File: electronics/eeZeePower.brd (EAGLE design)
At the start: 25.9 x 12.7 mm, 12 parts

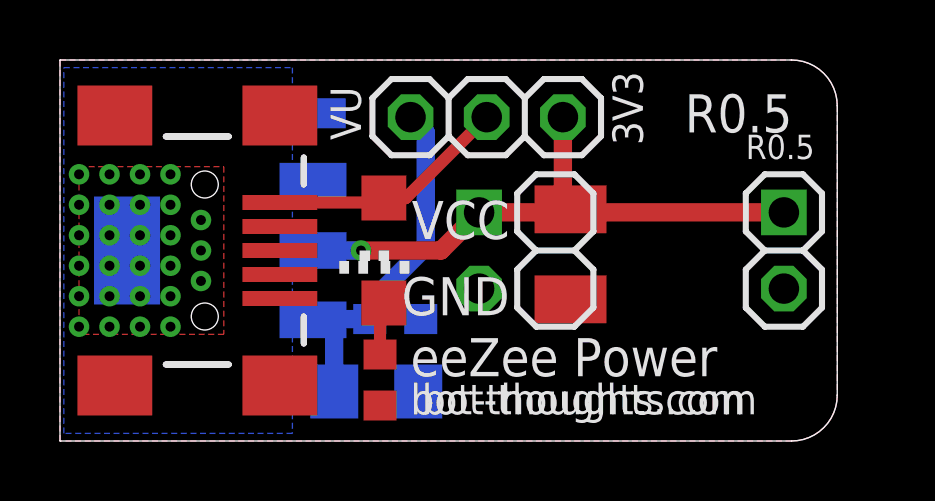
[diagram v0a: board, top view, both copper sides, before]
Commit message: modified logo to polygons, arcs; minor tweaks, moved url
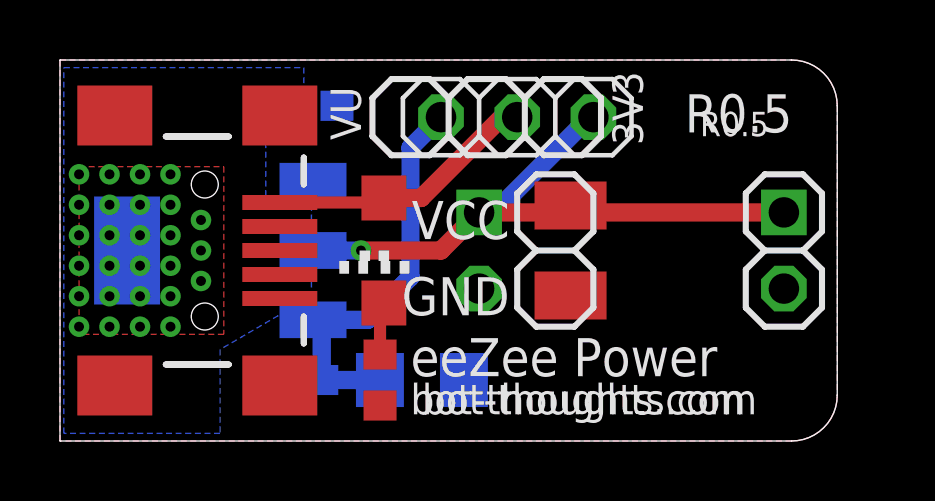
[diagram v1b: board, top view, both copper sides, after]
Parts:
- removed U$3: BOT-THOUGHTS-LOGO-MD, bt:BTLOGOM
- added U$2: BTLOGO-LOGO-MD, bt:BTLOGOM
- moved C2 3.88 mm to (7.87, 2.03), turned to 0 degrees
- moved C1 1.57 mm to (12.1, 2.03)
- moved JP10 1.02 mm to (15.2, 10.8)
- moved C3 0.36 mm to (8.38, 11.2)
- moved C4 0.13 mm to (17.0, 6.35)
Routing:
- net VOUT: track 20.4 -> 22.4 mm
- net VIN: track 12.6 -> 13.7 mm
- net VBUS: track 8.08 -> 9.09 mm
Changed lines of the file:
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@@
 <setting verticaltext="up"/>
 </settings>
-<grid distance="0.8" unitdist="mil" unit="mil" style="lines" multiple="1" display="yes" altdistance="0.01" altunitdist="inch" altunit="inch"/>
+<grid distance="0.005" unitdist="inch" unit="inch" style="lines" multiple="1" display="yes" altdistance="0.01" altunitdist="inch" altunit="inch"/>
 <layers>
 <layer number="1" name="Top" color="4" fill="1" visible="yes" active="yes"/>
@@
 <wire x1="24.384" y1="12.7" x2="0" y2="12.7" width="0" layer="20"/>
 <wire x1="0" y1="12.7" x2="0" y2="0" width="0" layer="20"/>
-<text x="19.304" y="10.033" size="1.016" layer="27" font="vector" rot="R90">VU</text>
+<text x="20.32" y="10.033" size="1.016" layer="27" font="vector" rot="R90">VU</text>
 <text x="12.319" y="2.159" size="1.27" layer="27" font="vector">eeZee Power</text>
 <text x="12.065" y="0.889" size="1.016" layer="25" font="vector">bot-thoughts.com</text>
-<text x="22.86" y="9.398" size="0.8128" layer="25" font="vector">R0.5</text>
+<text x="21.336" y="10.16" size="0.8128" layer="25" font="vector">R0.5</text>
 <text x="22.86" y="8.128" size="1.27" layer="27" font="vector" rot="R180">VCC</text>
 <text x="22.86" y="5.588" size="1.27" layer="27" font="vector" rot="R180">GND</text>
-<text x="10.16" y="9.525" size="1.016" layer="27" font="vector" rot="R90">3V3</text>
+<text x="11.176" y="9.525" size="1.016" layer="27" font="vector" rot="R90">3V3</text>
 <text x="11.684" y="0.889" size="1.016" layer="121" font="vector" ratio="20">bot-thoughts.com</text>
 <text x="20.828" y="10.287" size="1.27" layer="121" font="vector" ratio="16">R0.5</text>
@@
 <text x="14.986" y="5.461" size="1.27" layer="121" font="vector" ratio="16" rot="R180">GND</text>
 <text x="18.415" y="12.319" size="1.016" layer="121" font="vector" ratio="20" rot="R270">3V3</text>
-<text x="15.494" y="6.35" size="0.8128" layer="26" font="vector" rot="MR90" align="bottom-center">CC-BY-SA</text>
-<text x="21.1734375" y="6.2484" size="1.016" layer="26" font="vector" rot="MR90" align="bottom-center">is.gd/MTPmIU</text>
+<text x="15.748" y="6.35" size="0.8128" layer="26" font="vector" rot="MR90" align="bottom-center">CC-BY-SA</text>
+<text x="19.9136" y="1.1074375" size="1.016" layer="26" font="vector" rot="MR0" align="bottom-center">is.gd/MTPmIU</text>
 </plain>
 <attributes>
@@
 <attribute name="VALUE" x="5.5245" y="7.4295" size="0.4064" layer="28" rot="MR270"/>
 </element>
-<element name="JP10" library="pinhead-2" package="1X03-S" value="SEL" x="14.224" y="10.795" smashed="yes"/>
+<element name="JP10" library="pinhead-2" package="1X03-S" value="SEL" x="15.24" y="10.795" smashed="yes"/>
 <element name="LED1" library="led" package="CHIPLED_1206" value="" x="10.795" y="6.35" smashed="yes" rot="R180">
 <attribute name="VALUE" x="8.255" y="7.62" size="1.27" layer="27" rot="R270"/>
 </element>
-<element name="C2" library="rcl" package="C0603" value="0.1uF" x="11.176" y="4.064" smashed="yes" rot="MR180"/>
-<element name="C4" library="rcl" package="SMC_B" value="100uF" x="17.018" y="6.223" smashed="yes" rot="R270"/>
+<element name="C2" library="rcl" package="C0603" value="0.1uF" x="7.874" y="2.032" smashed="yes" rot="MR0"/>
+<element name="C4" library="rcl" package="SMC_B" value="100uF" x="17.018" y="6.35" smashed="yes" rot="R270"/>
 <element name="R1" library="resistor" package="R0603" value="" x="10.668" y="2.032" smashed="yes" rot="R90">
 <attribute name="VALUE" x="12.7" y="1.143" size="1.27" layer="27" rot="R90"/>
 </element>
-<element name="C1" library="rcl" package="C1206" value="10uF" x="10.541" y="1.651" smashed="yes" rot="MR180"/>
-<element name="C3" library="rcl" package="C0603" value="0.1uF" x="8.128" y="10.922" smashed="yes" rot="MR180"/>
+<element name="C1" library="rcl" package="C1206" value="10uF" x="12.065" y="2.032" smashed="yes" rot="MR180"/>
+<element name="C3" library="rcl" package="C0603" value="0.1uF" x="8.382" y="11.176" smashed="yes" rot="MR180"/>
 <element name="JP3" library="pinhead-2" package="1X02-S" value="" x="13.97" y="6.35" smashed="yes" rot="MR270">
 <attribute name="VALUE" x="17.145" y="8.89" size="1.27" layer="28" rot="MR270"/>
@@
 </element>
 <element name="U$1" library="SparkFun" package="USB-MINIB" value="USB-MINIB-5PIN" x="4.826" y="6.35" smashed="yes"/>
-<element name="U$3" library="bt" package="BTLOGOM" value="BOT-THOUGHTS-LOGO-MD" x="17.8409625" y="6.217921875" rot="MR90"/>
+<element name="U$2" library="bt" package="BTLOGOM" value="BTLOGO-LOGO-MD" x="16.891" y="6.35" rot="MR90"/>
 </elements>
 <signals>
@@
 <contactref element="C1" pad="1"/>
 <contactref element="JP10" pad="1"/>
-<wire x1="9.141" y1="1.651" x2="9.141" y2="3.807" width="0.6096" layer="16"/>
-<wire x1="9.141" y1="3.807" x2="9.144" y2="3.81" width="0.6096" layer="16"/>
-<wire x1="9.144" y1="3.81" x2="8.6614" y2="3.81" width="0.6096" layer="16"/>
-<wire x1="8.6614" y1="3.81" x2="8.4328" y2="4.0386" width="0.6096" layer="16"/>
-<wire x1="10.326" y1="4.064" x2="8.4582" y2="4.064" width="0.6096" layer="16"/>
-<wire x1="8.4582" y1="4.064" x2="8.4328" y2="4.0386" width="0.6096" layer="16"/>
-<wire x1="11.684" y1="10.795" x2="12.192" y2="10.287" width="0.6096" layer="16"/>
-<wire x1="12.192" y1="10.287" x2="12.192" y2="6.477" width="0.6096" layer="16"/>
-<wire x1="12.192" y1="6.477" x2="10.414" y2="4.699" width="0.6096" layer="16"/>
-<wire x1="10.414" y1="4.699" x2="10.414" y2="4.152" width="0.6096" layer="16"/>
-<wire x1="10.414" y1="4.152" x2="10.326" y2="4.064" width="0.6096" layer="16"/>
+<wire x1="12.7" y1="10.795" x2="11.684" y2="9.779" width="0.6096" layer="16"/>
+<wire x1="11.684" y1="9.779" x2="11.684" y2="5.464" width="0.6096" layer="16"/>
+<wire x1="8.4328" y1="4.0386" x2="10.2586" y2="4.0386" width="0.6096" layer="16"/>
+<wire x1="10.2586" y1="4.0386" x2="11.684" y2="5.464" width="0.6096" layer="16"/>
+<wire x1="8.724" y1="2.032" x2="8.724" y2="3.7474" width="0.6096" layer="16"/>
+<wire x1="8.724" y1="3.7474" x2="8.4328" y2="4.0386" width="0.6096" layer="16"/>
+<wire x1="8.724" y1="2.032" x2="10.665" y2="2.032" width="0.6096" layer="16"/>
 </signal>
 <signal name="GND">
@@
 <via x="3.683" y="6.858" extent="1-16" drill="0.3302"/>
 <via x="0.635" y="7.874" extent="1-16" drill="0.3302"/>
-<polygon width="0.4064" layer="16" isolate="0.3048">
+<polygon width="0.254" layer="16" isolate="0.3048">
 <vertex x="0.127" y="12.446"/>
-<vertex x="7.747" y="12.446"/>
-<vertex x="7.747" y="0.254"/>
+<vertex x="8.128" y="12.446"/>
+<vertex x="8.128" y="10.922"/>
+<vertex x="6.858" y="10.922"/>
+<vertex x="6.858" y="7.874"/>
+<vertex x="8.382" y="7.874"/>
+<vertex x="8.382" y="4.826"/>
+<vertex x="5.334" y="3.048"/>
+<vertex x="5.334" y="0.254"/>
 <vertex x="0.127" y="0.254"/>
 </polygon>
@@
 <via x="4.699" y="7.366" extent="1-16" drill="0.3302"/>
 <wire x1="13.97" y1="7.62" x2="16.407" y2="7.62" width="0.6096" layer="1"/>
-<wire x1="16.407" y1="7.62" x2="17.018" y2="7.723" width="0.6096" layer="1"/>
+<wire x1="16.407" y1="7.62" x2="17.018" y2="7.85" width="0.6096" layer="1"/>
 <wire x1="24.13" y1="7.62" x2="17.272" y2="7.62" width="0.6096" layer="1"/>
 <wire x1="17.272" y1="7.62" x2="17.145" y2="7.747" width="0.6096" layer="1"/>
 <wire x1="17.145" y1="7.747" x2="16.534" y2="7.747" width="0.6096" layer="1"/>
-<wire x1="16.534" y1="7.747" x2="17.018" y2="7.723" width="0.6096" layer="1"/>
-<wire x1="16.764" y1="10.795" x2="16.764" y2="7.977" width="0.6096" layer="1"/>
-<wire x1="16.764" y1="7.977" x2="17.018" y2="7.723" width="0.6096" layer="1"/>
+<wire x1="16.534" y1="7.747" x2="17.018" y2="7.85" width="0.6096" layer="1"/>
 <wire x1="8.4328" y1="6.35" x2="10.033" y2="6.35" width="0.6096" layer="16"/>
 <via x="10.033" y="6.35" extent="1-16" drill="0.3302"/>
 <wire x1="10.033" y1="6.35" x2="12.7" y2="6.35" width="0.6096" layer="1"/>
 <wire x1="12.7" y1="6.35" x2="13.97" y2="7.62" width="0.6096" layer="1"/>
+<wire x1="17.78" y1="10.795" x2="17.653" y2="10.795" width="0.6096" layer="16"/>
+<wire x1="17.653" y1="10.795" x2="14.478" y2="7.62" width="0.6096" layer="16"/>
+<wire x1="14.478" y1="7.62" x2="13.97" y2="7.62" width="0.6096" layer="16"/>
 </signal>
 <signal name="VBUS">
 <contactref element="JP10" pad="2"/>
 <contactref element="LED1" pad="A"/>
-<wire x1="10.795" y1="8.1" x2="11.529" y2="8.1" width="0.4064" layer="1"/>
-<wire x1="11.529" y1="8.1" x2="14.224" y2="10.795" width="0.4064" layer="1"/>
 <contactref element="U$1" pad="VBUS"/>
 <wire x1="7.326" y1="7.95" x2="10.645" y2="7.95" width="0.4064" layer="1"/>
 <wire x1="10.645" y1="7.95" x2="10.795" y2="8.1" width="0.4064" layer="1"/>
+<wire x1="10.795" y1="8.1" x2="12.037" y2="8.1" width="0.6096" layer="1"/>
+<wire x1="12.037" y1="8.1" x2="14.732" y2="10.795" width="0.6096" layer="1"/>
+<wire x1="14.732" y1="10.795" x2="15.24" y2="10.795" width="0.6096" layer="1"/>
 </signal>
 </signals>
